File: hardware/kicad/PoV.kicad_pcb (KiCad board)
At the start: 2 copper layers, 9 parts, among them SW1 SW_DPDT_x2, U1 ATtiny85-20PU

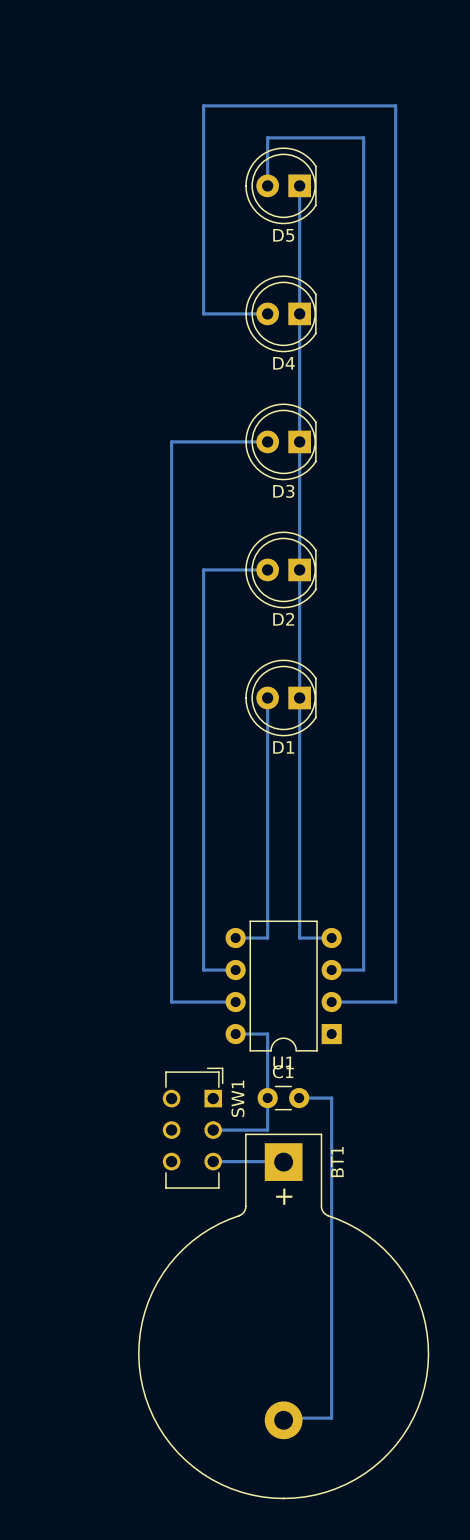
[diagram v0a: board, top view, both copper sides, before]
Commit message: added missed route on pcb
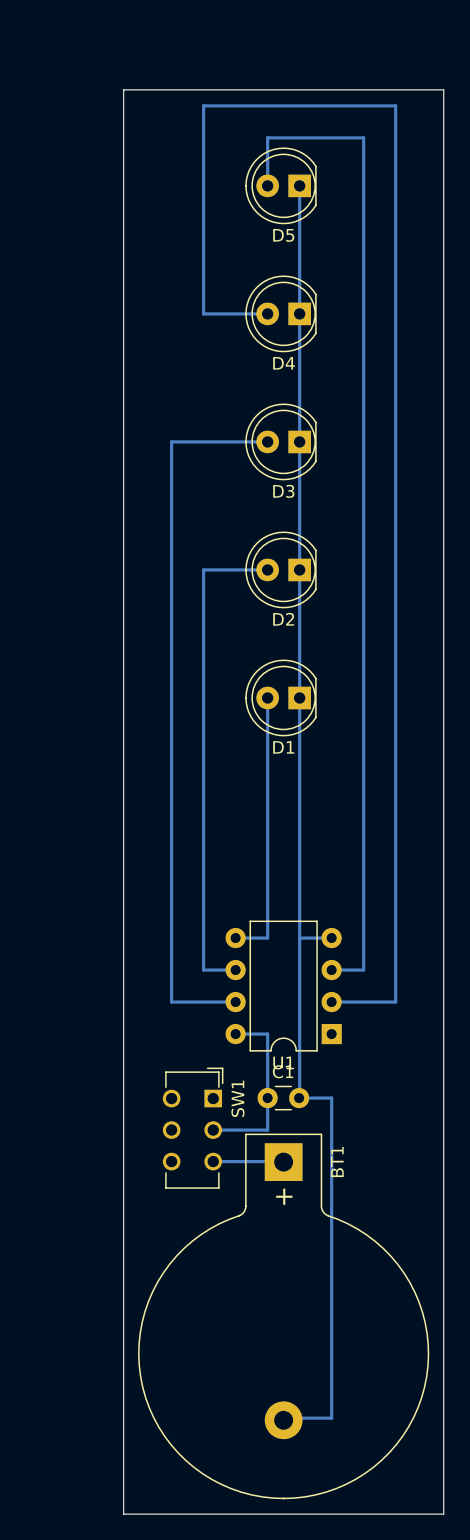
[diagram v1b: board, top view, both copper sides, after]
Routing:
- net Net-(BT1-Pad2): track 94.1 -> 106.8 mm
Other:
- board outline added: 25.4 x 113 mm

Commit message: improved design
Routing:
- net Net-(D5-Pad2): track 80.0 -> 90.2 mm
- net Net-(D4-Pad2): track 113.0 -> 118.1 mm
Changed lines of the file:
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@@
     (thickness 1.6)
     (drawings 4)
-    (tracks 35)
+    (tracks 36)
     (zones 0)
     (modules 9)
@@
   )
   (page A4)
+  (title_block
+    (title PoV)
+    (date 2021-10-01)
+    (rev 1)
+    (company "Filippo Sallemi")
+  )
   (layers
     (0 F.Cu signal)
@@
   (segment (start 160.02 116.84) (end 165.1 116.84) (width 0.25) (layer B.Cu) (net 7))
   (segment (start 165.1 116.84) (end 165.1 45.72) (width 0.25) (layer B.Cu) (net 7))
-  (segment (start 165.1 45.72) (end 149.86 45.72) (width 0.25) (layer B.Cu) (net 7))
-  (segment (start 149.86 45.72) (end 149.86 62.23) (width 0.25) (layer B.Cu) (net 7))
-  (segment (start 149.86 62.23) (end 154.94 62.23) (width 0.25) (layer B.Cu) (net 7))
+  (segment (start 165.1 45.72) (end 147.32 45.72) (width 0.25) (layer B.Cu) (net 7))
+  (segment (start 147.32 45.72) (end 147.32 62.23) (width 0.25) (layer B.Cu) (net 7))
+  (segment (start 147.32 62.23) (end 154.94 62.23) (width 0.25) (layer B.Cu) (net 7))
   (segment (start 160.02 114.3) (end 162.56 114.3) (width 0.25) (layer B.Cu) (net 8))
   (segment (start 162.56 114.3) (end 162.56 48.26) (width 0.25) (layer B.Cu) (net 8))
-  (segment (start 162.56 48.26) (end 154.94 48.26) (width 0.25) (layer B.Cu) (net 8))
-  (segment (start 154.94 48.26) (end 154.94 52.07) (width 0.25) (layer B.Cu) (net 8))
+  (segment (start 154.94 52.07) (end 149.86 52.07) (width 0.25) (layer B.Cu) (net 8))
+  (segment (start 149.86 52.07) (end 149.86 48.26) (width 0.25) (layer B.Cu) (net 8))
+  (segment (start 149.86 48.26) (end 162.56 48.26) (width 0.25) (layer B.Cu) (net 8))
 )

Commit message: improved design
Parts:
- moved BT1 9.16 mm to (148.6, 124.5)
- moved C1 9.16 mm to (147.3, 119.4)
- moved SW1 9.16 mm to (143.0, 119.4)
- moved U1 9.16 mm to (152.4, 114.3)
- moved D1 9.16 mm to (149.9, 87.6)
- moved D2 9.16 mm to (149.9, 77.5)
- moved D3 9.16 mm to (149.9, 67.3)
- moved D4 9.16 mm to (149.9, 57.1)
- moved D5 9.16 mm to (149.9, 47.0)
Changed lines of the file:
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@@
   )
   (module LED_THT:LED_D5.0mm (layer F.Cu)
-    (at 157.48 72.39 180)
+    (at 149.86 67.31 180)
     (descr "LED, diameter 5.0mm, 2 pins, http://cdn-reichelt.de/documents/datenblatt/A500/LL-504BC2E-009.pdf")
     (tags "LED diameter 5.0mm 2 pins")
@@
   )
   (module Battery:BatteryHolder_Keystone_103_1x20mm (layer F.Cu)
-    (at 156.21 129.54 270)
+    (at 148.59 124.46 270)
     (descr http://www.keyelco.com/product-pdf.cfm?p=719)
     (tags "Keystone type 103 battery holder")
@@
   )
   (module Capacitor_THT:C_Disc_D3.0mm_W1.6mm_P2.50mm (layer F.Cu)
-    (at 154.94 124.46)
+    (at 147.32 119.38)
     (descr "C, Disc series, Radial, pin pitch=2.50mm, , diameter*width=3.0*1.6mm^2, Capacitor, http://www.vishay.com/docs/45233/krseries.pdf")
     (tags "C Disc series Radial pin pitch 2.50mm  diameter 3.0mm width 1.6mm Capacitor")
@@
   )
   (module LED_THT:LED_D5.0mm (layer F.Cu)
-    (at 157.48 92.71 180)
+    (at 149.86 87.63 180)
     (descr "LED, diameter 5.0mm, 2 pins, http://cdn-reichelt.de/documents/datenblatt/A500/LL-504BC2E-009.pdf")
     (tags "LED diameter 5.0mm 2 pins")
@@
   )
   (module LED_THT:LED_D5.0mm (layer F.Cu)
-    (at 157.48 82.55 180)
+    (at 149.86 77.47 180)
     (descr "LED, diameter 5.0mm, 2 pins, http://cdn-reichelt.de/documents/datenblatt/A500/LL-504BC2E-009.pdf")
     (tags "LED diameter 5.0mm 2 pins")
@@
   )
   (module LED_THT:LED_D5.0mm (layer F.Cu)
-    (at 157.48 62.23 180)
+    (at 149.86 57.15 180)
     (descr "LED, diameter 5.0mm, 2 pins, http://cdn-reichelt.de/documents/datenblatt/A500/LL-504BC2E-009.pdf")
     (tags "LED diameter 5.0mm 2 pins")
@@
   )
   (module LED_THT:LED_D5.0mm (layer F.Cu)
-    (at 157.48 52.07 180)
+    (at 149.86 46.99 180)
     (descr "LED, diameter 5.0mm, 2 pins, http://cdn-reichelt.de/documents/datenblatt/A500/LL-504BC2E-009.pdf")
     (tags "LED diameter 5.0mm 2 pins")
@@
   )
   (module Button_Switch_THT:SW_CuK_JS202011AQN_DPDT_Angled (layer F.Cu)
-    (at 150.62 124.5 270)
+    (at 143 119.42 270)
     (descr "CuK sub miniature slide switch, JS series, DPDT, right angle, http://www.ckswitches.com/media/1422/js.pdf")
     (tags "switch DPDT")
@@
   )
   (module Package_DIP:DIP-8_W7.62mm (layer F.Cu)
-    (at 160.02 119.38 180)
+    (at 152.4 114.3 180)
     (descr "8-lead though-hole mounted DIP package, row spacing 7.62 mm (300 mils)")
     (tags "THT DIP DIL PDIP 2.54mm 7.62mm 300mil")
@@
     )
   )
-  (gr_line (start 168.91 44.45) (end 168.91 157.48) (layer Edge.Cuts) (width 0.1))
-  (gr_line (start 143.51 44.45) (end 168.91 44.45) (layer Edge.Cuts) (width 0.1))
-  (gr_line (start 143.51 157.48) (end 143.51 44.45) (layer Edge.Cuts) (width 0.1))
-  (gr_line (start 168.91 157.48) (end 143.51 157.48) (layer Edge.Cuts) (width 0.1))
-  (segment (start 157.44 124.46) (end 160.02 124.46) (width 0.25) (layer B.Cu) (net 1))
-  (segment (start 160.02 124.46) (end 160.02 149.86) (width 0.25) (layer B.Cu) (net 1))
-  (segment (start 156.38 149.86) (end 156.21 150.03) (width 0.25) (layer B.Cu) (net 1))
-  (segment (start 160.02 149.86) (end 156.38 149.86) (width 0.25) (layer B.Cu) (net 1))
-  (segment (start 157.48 52.07) (end 157.48 62.23) (width 0.25) (layer B.Cu) (net 1))
-  (segment (start 157.48 62.23) (end 157.48 72.39) (width 0.25) (layer B.Cu) (net 1))
-  (segment (start 157.48 72.39) (end 157.48 82.55) (width 0.25) (layer B.Cu) (net 1))
-  (segment (start 157.48 82.55) (end 157.48 92.71) (width 0.25) (layer B.Cu) (net 1))
-  (segment (start 157.48 92.71) (end 157.48 111.76) (width 0.25) (layer B.Cu) (net 1))
-  (segment (start 157.48 111.76) (end 160.02 111.76) (width 0.25) (layer B.Cu) (net 1))
-  (segment (start 157.48 124.42) (end 157.44 124.46) (width 0.25) (layer B.Cu) (net 1))
-  (segment (start 157.48 111.76) (end 157.48 124.42) (width 0.25) (layer B.Cu) (net 1))
-  (segment (start 156.17 129.5) (end 156.21 129.54) (width 0.25) (layer B.Cu) (net 2))
-  (segment (start 150.62 129.5) (end 156.17 129.5) (width 0.25) (layer B.Cu) (net 2))
-  (segment (start 150.62 127) (end 154.94 127) (width 0.25) (layer B.Cu) (net 3))
-  (segment (start 154.94 127) (end 154.94 124.46) (width 0.25) (layer B.Cu) (net 3))
-  (segment (start 152.4 119.38) (end 154.94 119.38) (width 0.25) (layer B.Cu) (net 3))
-  (segment (start 154.94 119.38) (end 154.94 124.46) (width 0.25) (layer B.Cu) (net 3))
-  (segment (start 154.94 92.71) (end 154.94 111.76) (width 0.25) (layer B.Cu) (net 4))
-  (segment (start 154.94 111.76) (end 152.4 111.76) (width 0.25) (layer B.Cu) (net 4))
-  (segment (start 152.4 114.3) (end 149.86 114.3) (width 0.25) (layer B.Cu) (net 5))
-  (segment (start 149.86 114.3) (end 149.86 82.55) (width 0.25) (layer B.Cu) (net 5))
-  (segment (start 149.86 82.55) (end 154.94 82.55) (width 0.25) (layer B.Cu) (net 5))
-  (segment (start 152.4 116.84) (end 147.32 116.84) (width 0.25) (layer B.Cu) (net 6))
-  (segment (start 147.32 116.84) (end 147.32 72.39) (width 0.25) (layer B.Cu) (net 6))
-  (segment (start 147.32 72.39) (end 154.94 72.39) (width 0.25) (layer B.Cu) (net 6))
-  (segment (start 160.02 116.84) (end 165.1 116.84) (width 0.25) (layer B.Cu) (net 7))
-  (segment (start 165.1 116.84) (end 165.1 45.72) (width 0.25) (layer B.Cu) (net 7))
-  (segment (start 165.1 45.72) (end 147.32 45.72) (width 0.25) (layer B.Cu) (net 7))
-  (segment (start 147.32 45.72) (end 147.32 62.23) (width 0.25) (layer B.Cu) (net 7))
-  (segment (start 147.32 62.23) (end 154.94 62.23) (width 0.25) (layer B.Cu) (net 7))
-  (segment (start 160.02 114.3) (end 162.56 114.3) (width 0.25) (layer B.Cu) (net 8))
-  (segment (start 162.56 114.3) (end 162.56 48.26) (width 0.25) (layer B.Cu) (net 8))
-  (segment (start 154.94 52.07) (end 149.86 52.07) (width 0.25) (layer B.Cu) (net 8))
-  (segment (start 149.86 52.07) (end 149.86 48.26) (width 0.25) (layer B.Cu) (net 8))
-  (segment (start 149.86 48.26) (end 162.56 48.26) (width 0.25) (layer B.Cu) (net 8))
+  (gr_line (start 161.29 39.37) (end 161.29 152.4) (layer Edge.Cuts) (width 0.1))
+  (gr_line (start 135.89 39.37) (end 161.29 39.37) (layer Edge.Cuts) (width 0.1))
+  (gr_line (start 135.89 152.4) (end 135.89 39.37) (layer Edge.Cuts) (width 0.1))
+  (gr_line (start 161.29 152.4) (end 135.89 152.4) (layer Edge.Cuts) (width 0.1))
+  (segment (start 149.82 119.38) (end 152.4 119.38) (width 0.25) (layer B.Cu) (net 1))
+  (segment (start 152.4 119.38) (end 152.4 144.78) (width 0.25) (layer B.Cu) (net 1))
+  (segment (start 148.76 144.78) (end 148.59 144.95) (width 0.25) (layer B.Cu) (net 1))
+  (segment (start 152.4 144.78) (end 148.76 144.78) (width 0.25) (layer B.Cu) (net 1))
+  (segment (start 149.86 46.99) (end 149.86 57.15) (width 0.25) (layer B.Cu) (net 1))
+  (segment (start 149.86 57.15) (end 149.86 67.31) (width 0.25) (layer B.Cu) (net 1))
+  (segment (start 149.86 67.31) (end 149.86 77.47) (width 0.25) (layer B.Cu) (net 1))
+  (segment (start 149.86 77.47) (end 149.86 87.63) (width 0.25) (layer B.Cu) (net 1))
+  (segment (start 149.86 87.63) (end 149.86 106.68) (width 0.25) (layer B.Cu) (net 1))
+  (segment (start 149.86 106.68) (end 152.4 106.68) (width 0.25) (layer B.Cu) (net 1))
+  (segment (start 149.86 119.34) (end 149.82 119.38) (width 0.25) (layer B.Cu) (net 1))
+  (segment (start 149.86 106.68) (end 149.86 119.34) (width 0.25) (layer B.Cu) (net 1))
+  (segment (start 148.55 124.42) (end 148.59 124.46) (width 0.25) (layer B.Cu) (net 2))
+  (segment (start 143 124.42) (end 148.55 124.42) (width 0.25) (layer B.Cu) (net 2))
+  (segment (start 143 121.92) (end 147.32 121.92) (width 0.25) (layer B.Cu) (net 3))
+  (segment (start 147.32 121.92) (end 147.32 119.38) (width 0.25) (layer B.Cu) (net 3))
+  (segment (start 144.78 114.3) (end 147.32 114.3) (width 0.25) (layer B.Cu) (net 3))
+  (segment (start 147.32 114.3) (end 147.32 119.38) (width 0.25) (layer B.Cu) (net 3))
+  (segment (start 147.32 87.63) (end 147.32 106.68) (width 0.25) (layer B.Cu) (net 4))
+  (segment (start 147.32 106.68) (end 144.78 106.68) (width 0.25) (layer B.Cu) (net 4))
+  (segment (start 144.78 109.22) (end 142.24 109.22) (width 0.25) (layer B.Cu) (net 5))
+  (segment (start 142.24 109.22) (end 142.24 77.47) (width 0.25) (layer B.Cu) (net 5))
+  (segment (start 142.24 77.47) (end 147.32 77.47) (width 0.25) (layer B.Cu) (net 5))
+  (segment (start 144.78 111.76) (end 139.7 111.76) (width 0.25) (layer B.Cu) (net 6))
+  (segment (start 139.7 111.76) (end 139.7 67.31) (width 0.25) (layer B.Cu) (net 6))
+  (segment (start 139.7 67.31) (end 147.32 67.31) (width 0.25) (layer B.Cu) (net 6))
+  (segment (start 152.4 111.76) (end 157.48 111.76) (width 0.25) (layer B.Cu) (net 7))
+  (segment (start 157.48 111.76) (end 157.48 40.64) (width 0.25) (layer B.Cu) (net 7))
+  (segment (start 157.48 40.64) (end 139.7 40.64) (width 0.25) (layer B.Cu) (net 7))
+  (segment (start 139.7 40.64) (end 139.7 57.15) (width 0.25) (layer B.Cu) (net 7))
+  (segment (start 139.7 57.15) (end 147.32 57.15) (width 0.25) (layer B.Cu) (net 7))
+  (segment (start 152.4 109.22) (end 154.94 109.22) (width 0.25) (layer B.Cu) (net 8))
+  (segment (start 154.94 109.22) (end 154.94 43.18) (width 0.25) (layer B.Cu) (net 8))
+  (segment (start 147.32 46.99) (end 142.24 46.99) (width 0.25) (layer B.Cu) (net 8))
+  (segment (start 142.24 46.99) (end 142.24 43.18) (width 0.25) (layer B.Cu) (net 8))
+  (segment (start 142.24 43.18) (end 154.94 43.18) (width 0.25) (layer B.Cu) (net 8))
 )

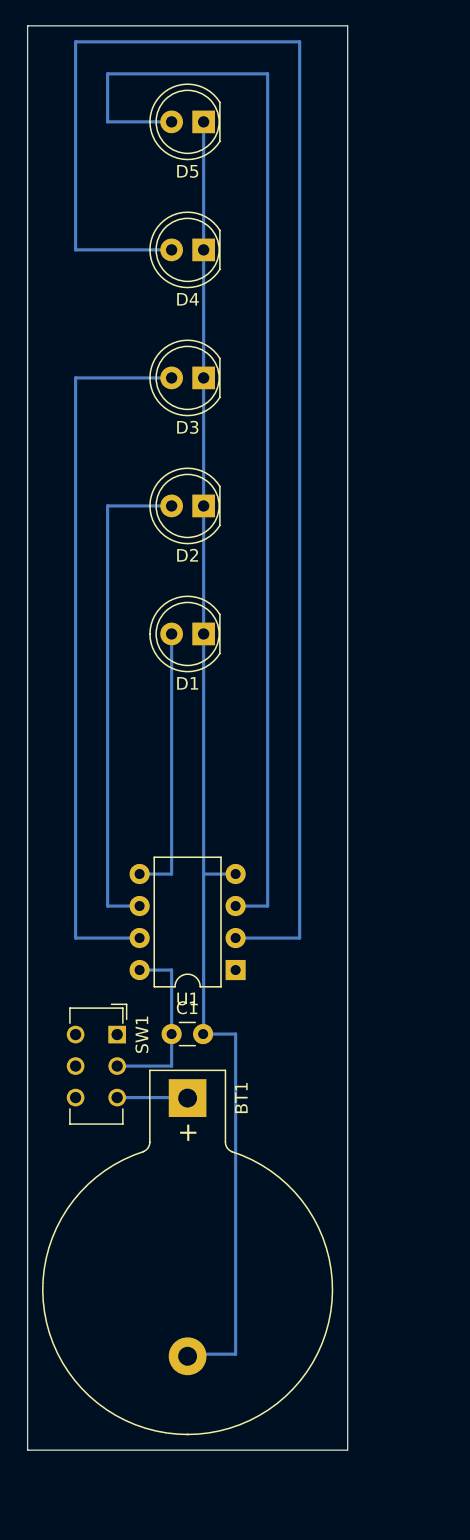
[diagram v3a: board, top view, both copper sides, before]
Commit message: now pov is programmable from board
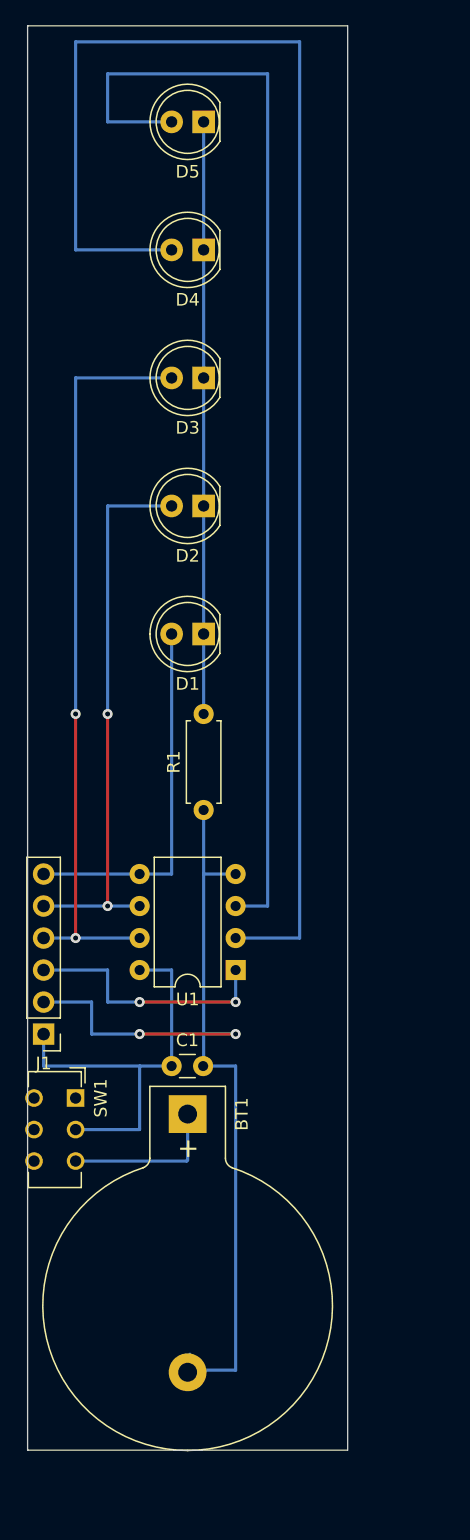
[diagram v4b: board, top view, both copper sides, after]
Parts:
- added J1: Conn_01x06_Male, Connector_PinHeader_2.54mm:PinHeader_1x06_P2.54mm_Vertical, F.Cu at (137.2, 119.4)
- added R1: R, Resistor_THT:R_Axial_DIN0207_L6.3mm_D2.5mm_P7.62mm_Horizontal, F.Cu at (149.9, 101.6)
- moved SW1 6.02 mm to (139.7, 124.5)
- moved C1 2.54 mm to (147.3, 121.9)
- moved BT1 1.27 mm to (148.6, 125.7)
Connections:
- net Net-(C1-Pad1) renamed VCC
- net Net-(D1-Pad2) renamed PB0
- net Net-(D2-Pad2) renamed PB1
- net Net-(D3-Pad2) renamed PB2
- net Net-(D4-Pad2) renamed PB3
- net Net-(D5-Pad2) renamed PB4
- BT1 pad 2: Net-(BT1-Pad2) -> GND
- C1 pad 2: Net-(BT1-Pad2) -> GND
- D1 pad 1: Net-(BT1-Pad2) -> Net-(D1-Pad1)
- D2 pad 1: Net-(BT1-Pad2) -> Net-(D1-Pad1)
- D3 pad 1: Net-(BT1-Pad2) -> Net-(D1-Pad1)
- D4 pad 1: Net-(BT1-Pad2) -> Net-(D1-Pad1)
- D5 pad 1: Net-(BT1-Pad2) -> Net-(D1-Pad1)
- SW1 pad 1: Net-(SW1-Pad1) -> (no net)
- U1 pad 1: Net-(U1-Pad1) -> PB5
- U1 pad 4: Net-(BT1-Pad2) -> GND
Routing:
- net Net-(BT1-Pad2): track 106.8 -> 0.00 mm
- net GND: track 0.00 -> 74.1 mm, vias 0 -> 2
- net Net-(D1-Pad1): track 0.00 -> 47.0 mm
- net PB5: track 0.00 -> 20.3 mm, vias 0 -> 2
- net VCC: track 14.5 -> 33.0 mm
- net PB0: track 21.6 -> 29.2 mm
- net Net-(BT1-Pad1): track 5.61 -> 12.6 mm
- net PB1: track 39.4 -> 44.4 mm, vias 0 -> 2
- net PB2: track 57.2 -> 59.7 mm, vias 0 -> 2
